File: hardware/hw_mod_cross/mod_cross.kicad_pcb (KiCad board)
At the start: 2 copper layers, 90.2 x 97.8 mm, 40 parts, among them J1 MOD_IN, J2 MOD, J3 MOD_OUT

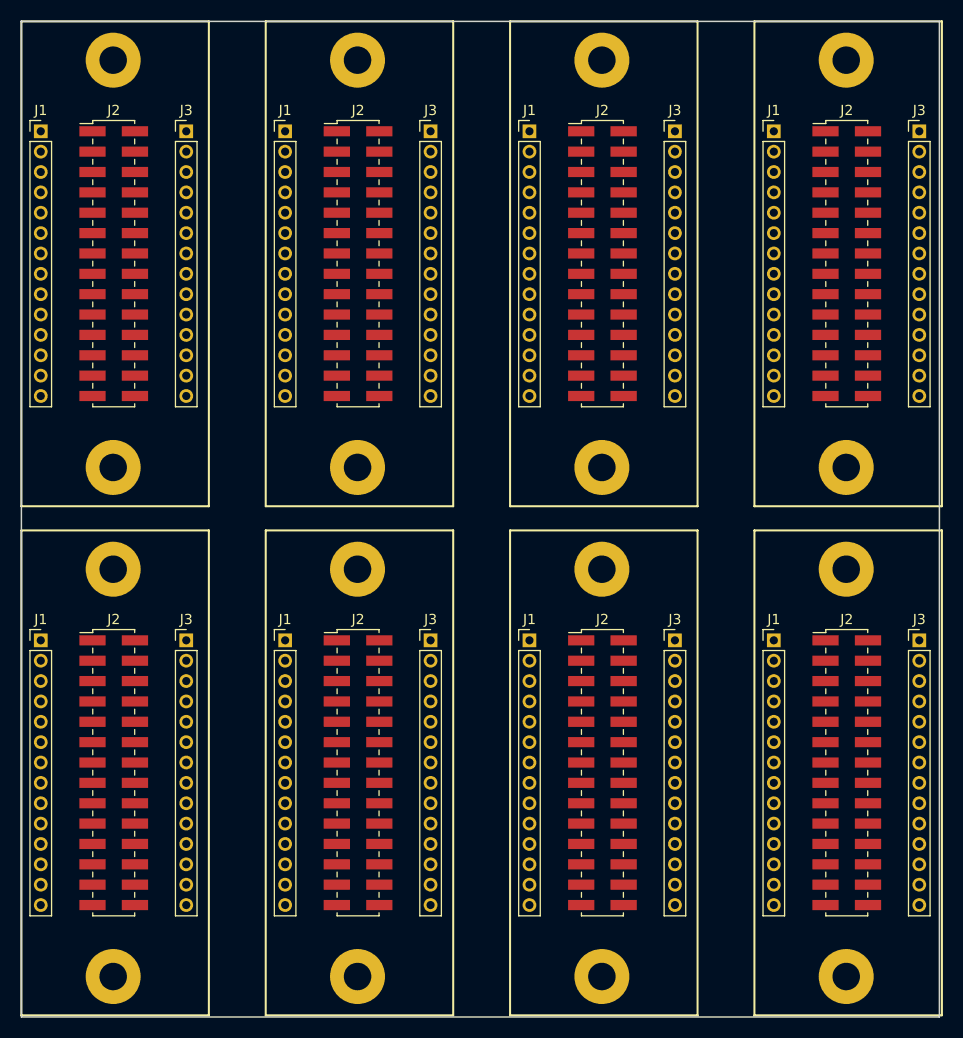
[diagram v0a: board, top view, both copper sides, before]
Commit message: Обновлена кросс-плата для модулей.
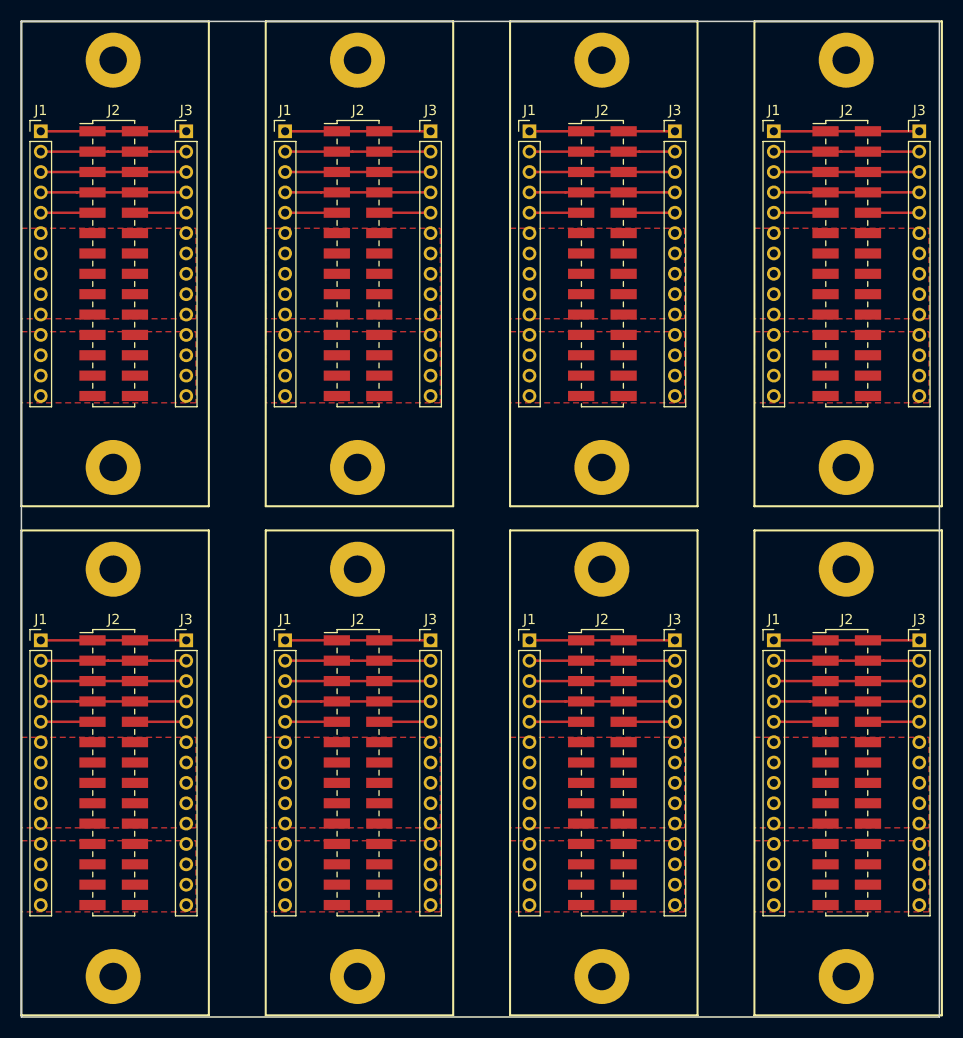
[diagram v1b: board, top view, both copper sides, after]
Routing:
- net SPI_SCK: track 0.00 -> 114.3 mm
- net SPI_MOSI: track 0.00 -> 114.3 mm
- net SPI_MISO: track 0.00 -> 114.3 mm
- net RESET: track 0.00 -> 114.3 mm
- net SEL_IN: track 0.00 -> 40.6 mm
- net SEL_OUT: track 0.00 -> 40.3 mm
- added copper zone on F.Cu, net VDD
- added copper zone on F.Cu, net VSS
